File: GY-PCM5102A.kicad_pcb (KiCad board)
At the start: 2 copper layers, 31.5 x 17 mm, 30 parts, among them J1 M-BUS, J2 FUN_AND_OUT, J3 AudioJack3, U1 PCM5102A, U2 ME6211C33M5, U3 ME6211C33M5

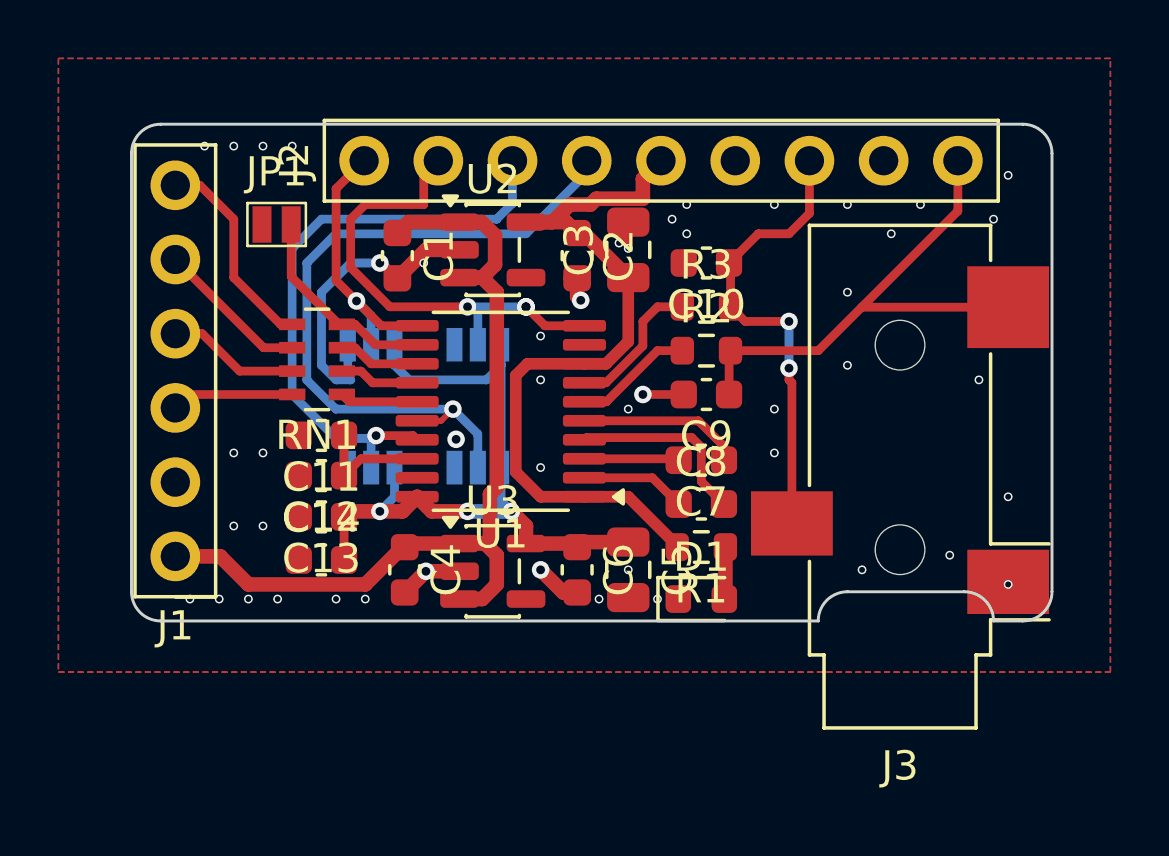
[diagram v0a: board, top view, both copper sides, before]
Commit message: feat: Add silkscreen. Change PCB color to magenta in 3D viewer.
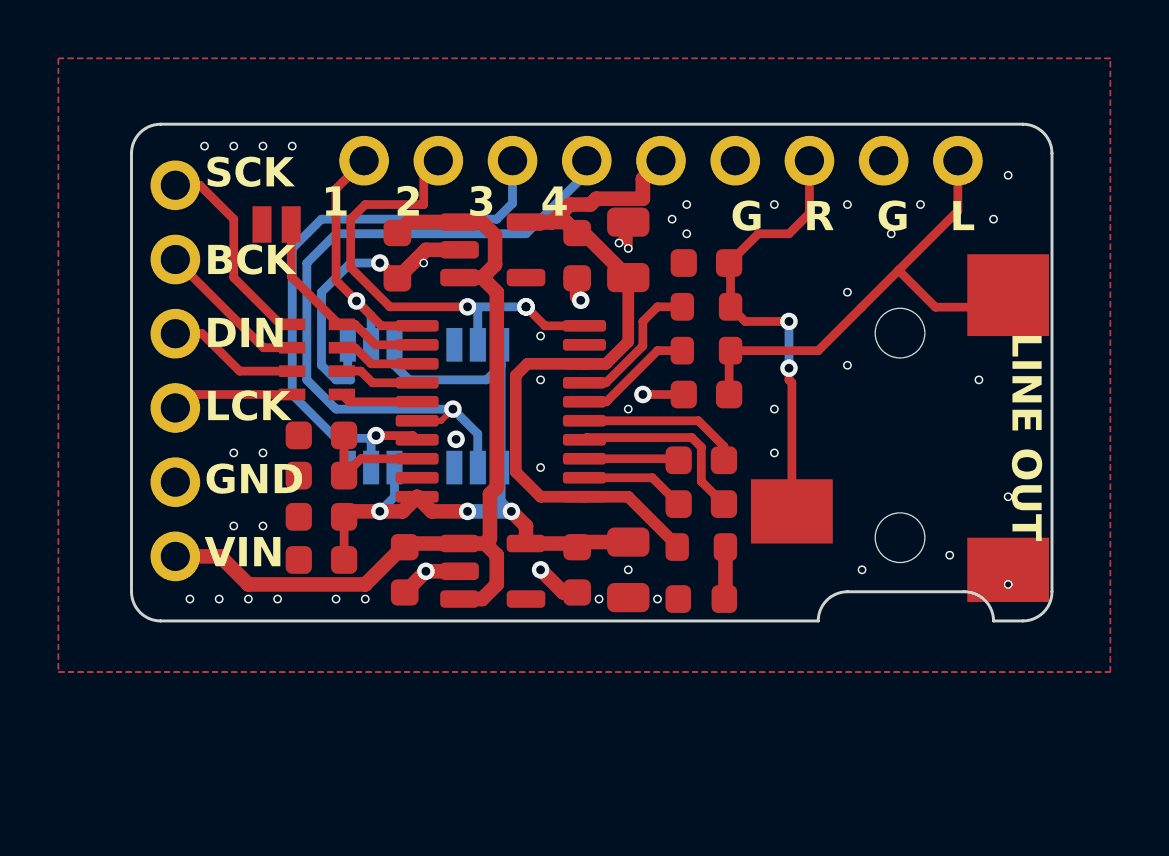
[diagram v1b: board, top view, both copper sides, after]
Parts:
- moved J3 0.41 mm to (129.8, 78.4)
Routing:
- net /OUTL: track 18.0 -> 17.3 mm
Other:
- board text added: "1"
- board text added: "2"
- board text added: "3"
- board text added: "4"
- board text added: "A3V3"
- board text added: "AGND"
- board text added: "BCK"
- board text added: "DEMP"
- board text added: "DIN"
- board text added: "FLT"
- board text added: "FMT"
- board text added: "G"
- board text added: "GND"
- board text added: "H1L"
- board text added: "H2L"
- board text added: "H3L"
- board text added: "H4L"
- board text added: "L"
- board text added: "LCK"
- board text added: "LINE OUT"
- board text added: "LROUT"
- board text added: "R"
- board text added: "ROUT"
- board text added: "SCK"
- board text added: "VIN"
- board text added: "XSMT"
